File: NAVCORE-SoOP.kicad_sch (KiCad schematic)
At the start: 195 parts, among them J1 USB-C, J11 SERIAL2 4P, J12 U.FL ANT, J14 FLOW 6P, J15 LED 3P, J16 BUZZ 2P, J17 SERVO 6P, J18 PYRO 2P, J19 SWD 4P, J2 ESC 8P, J20 TOUCH 2P, J3 GPS+I2C, J5 RC IN, J6 CAN 4P, J8 microSD, J9 I2C 4P, P41 TEL_5V, P44 TEL_PPS, P46 TEL_GND, P71 RF_5V, P72 RF_TX, P73 RF_RX, P74 RF_GND, Q1 AO3400A, Q3 AO3400A, Q4 WST4041, Q5 AO3400A, SW1 BOOT, SW2 RESET, U1 STM32H743VIT6, U10 TLV75533, U11 SN65HVD230, U12 USBLC6-2SC6, U13 MAX2112, U14 OPA2374, U17 74LVC1G17, U19 TMP119, U2 ICM-42688-P, U20 LMR33630A, U21 XC6206P332MR, U3 ICM-42605, U4 MS5611, U5 W25Q128JVSIQ, U8 LMR33630A, U9 AP2112K-3.3, Y1 8MHz, Y2 25MHz TCXO

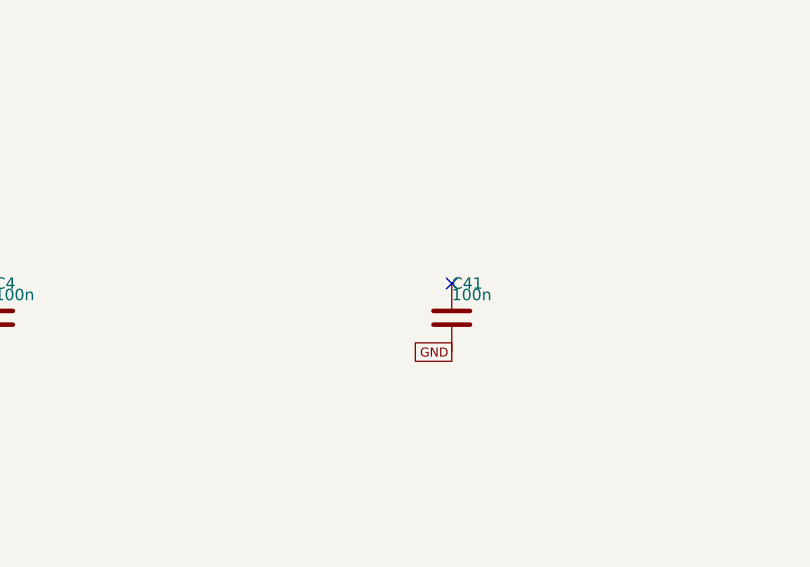
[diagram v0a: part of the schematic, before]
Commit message: give the payload and analogue rails real copper, put C41 on the CAN supply
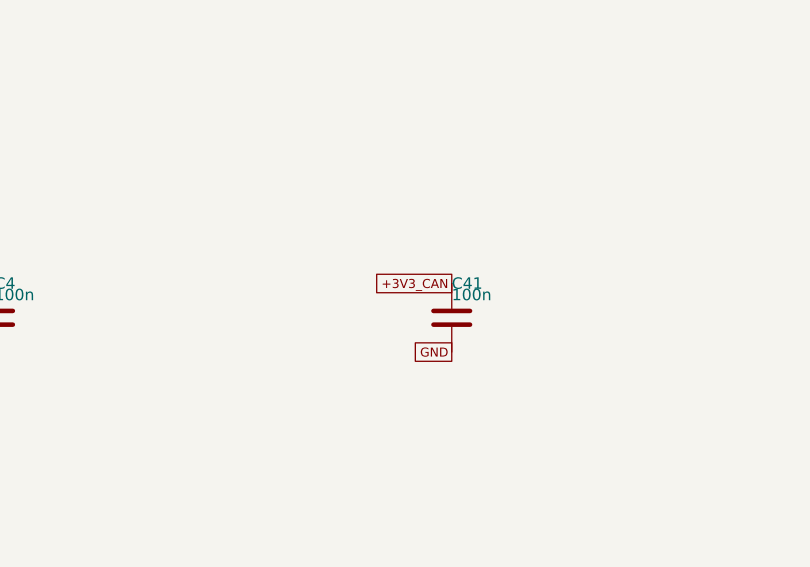
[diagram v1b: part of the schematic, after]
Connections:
- net +3V3_CAN: now also C41.1
- no-connect marks 44 -> 43
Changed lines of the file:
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@@
 		(instances (project "NAVCORE-SoOP" (path "/" (reference "C41") (unit 1))))
 	)
-	(no_connect (at 153.67 252.73))
+	(global_label "+3V3_CAN" (shape passive) (at 153.67 252.73 180)
+		(effects (font (size 1.0 1.0)) (justify right))
+	)
 	(global_label "GND" (shape passive) (at 153.67 260.35 180)
 		(effects (font (size 1.0 1.0)) (justify right))

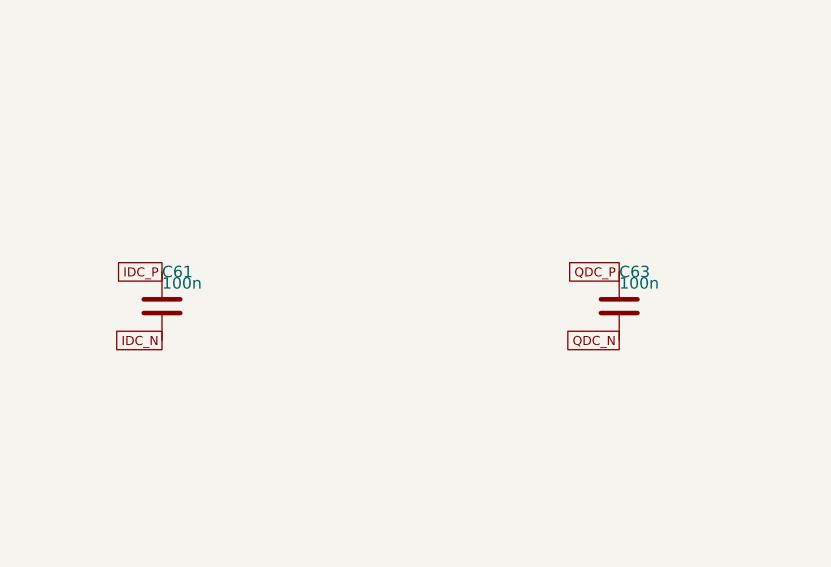
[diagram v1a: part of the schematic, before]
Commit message: fit 47 nF on the MAX2112 offset caps, as the datasheet asks
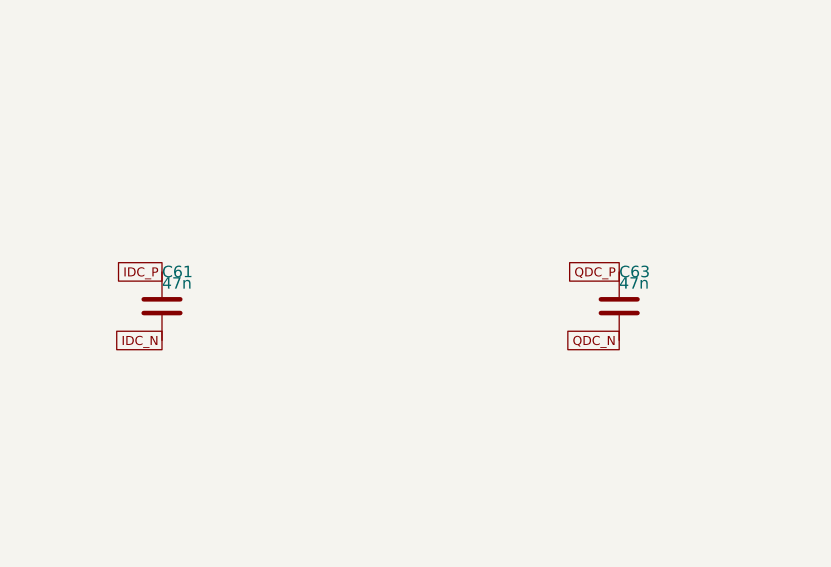
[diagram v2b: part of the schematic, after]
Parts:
- C61, C63: value 100n -> 47n
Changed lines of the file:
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@@
 		(exclude_from_sim no) (in_bom yes) (on_board yes) (dnp no)
 		(property "Reference" "C61" (at 1017.27 252.73 0) (effects (font (size 1.27 1.27)) (justify left)))
-		(property "Value" "100n" (at 1017.27 254.00 0) (effects (font (size 1.27 1.27)) (justify left)))
+		(property "Value" "47n" (at 1017.27 254.00 0) (effects (font (size 1.27 1.27)) (justify left)))
 		(property "Footprint" "Capacitor_SMD:C_0402_1005Metric" (at 1017.27 256.54 0) (effects (font (size 1.27 1.27)) hide))
 		(property "LCSC" "C1525" (at 1017.27 256.54 0) (effects (font (size 1.27 1.27)) hide))
@@
 		(exclude_from_sim no) (in_bom yes) (on_board yes) (dnp no)
 		(property "Reference" "C63" (at 1068.07 252.73 0) (effects (font (size 1.27 1.27)) (justify left)))
-		(property "Value" "100n" (at 1068.07 254.00 0) (effects (font (size 1.27 1.27)) (justify left)))
+		(property "Value" "47n" (at 1068.07 254.00 0) (effects (font (size 1.27 1.27)) (justify left)))
 		(property "Footprint" "Capacitor_SMD:C_0402_1005Metric" (at 1068.07 256.54 0) (effects (font (size 1.27 1.27)) hide))
 		(property "LCSC" "C1525" (at 1068.07 256.54 0) (effects (font (size 1.27 1.27)) hide))

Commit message: stop the artwork carrying part numbers that nothing checks
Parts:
- C61, C63: LCSC C1525 -> C82219
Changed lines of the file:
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@@
 		(property "Value" "47n" (at 1017.27 254.00 0) (effects (font (size 1.27 1.27)) (justify left)))
 		(property "Footprint" "Capacitor_SMD:C_0402_1005Metric" (at 1017.27 256.54 0) (effects (font (size 1.27 1.27)) hide))
-		(property "LCSC" "C1525" (at 1017.27 256.54 0) (effects (font (size 1.27 1.27)) hide))
+		(property "LCSC" "C82219" (at 1017.27 256.54 0) (effects (font (size 1.27 1.27)) hide))
 		(pin "1")
 		(pin "2")
@@
 		(property "Value" "47n" (at 1068.07 254.00 0) (effects (font (size 1.27 1.27)) (justify left)))
 		(property "Footprint" "Capacitor_SMD:C_0402_1005Metric" (at 1068.07 256.54 0) (effects (font (size 1.27 1.27)) hide))
-		(property "LCSC" "C1525" (at 1068.07 256.54 0) (effects (font (size 1.27 1.27)) hide))
+		(property "LCSC" "C82219" (at 1068.07 256.54 0) (effects (font (size 1.27 1.27)) hide))
 		(pin "1")
 		(pin "2")

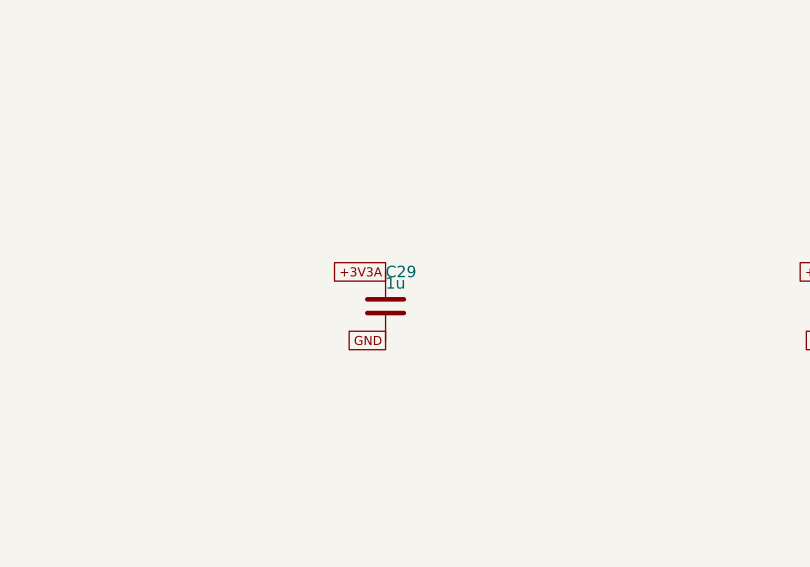
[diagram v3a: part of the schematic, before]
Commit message: widen C29 to 2u2 and sync the LCSC properties
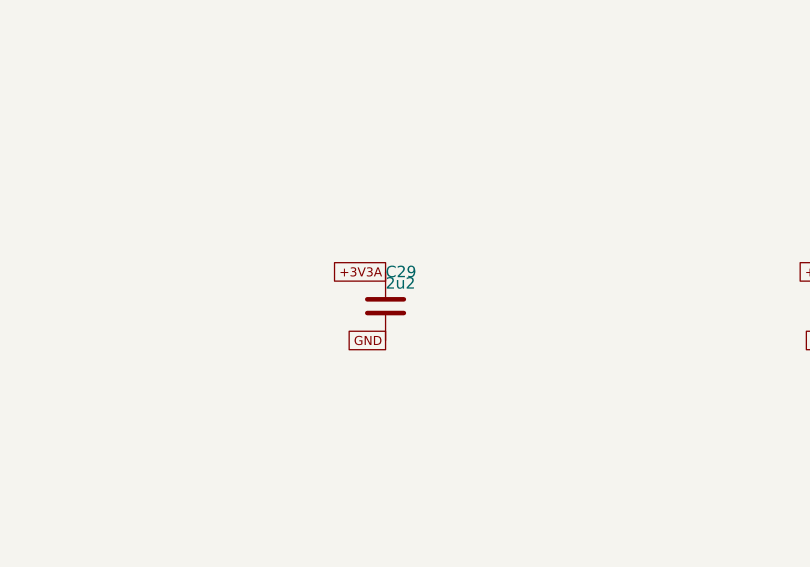
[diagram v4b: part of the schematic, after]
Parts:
- C29: value 1u -> 2u2; LCSC C52923 -> C12530
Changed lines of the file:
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@@
 		(exclude_from_sim no) (in_bom yes) (on_board yes) (dnp no)
 		(property "Reference" "C29" (at 999.49 207.01 0) (effects (font (size 1.27 1.27)) (justify left)))
-		(property "Value" "1u" (at 999.49 208.28 0) (effects (font (size 1.27 1.27)) (justify left)))
+		(property "Value" "2u2" (at 999.49 208.28 0) (effects (font (size 1.27 1.27)) (justify left)))
 		(property "Footprint" "Capacitor_SMD:C_0402_1005Metric" (at 999.49 210.82 0) (effects (font (size 1.27 1.27)) hide))
-		(property "LCSC" "C52923" (at 999.49 210.82 0) (effects (font (size 1.27 1.27)) hide))
+		(property "LCSC" "C12530" (at 999.49 210.82 0) (effects (font (size 1.27 1.27)) hide))
 		(pin "1")
 		(pin "2")

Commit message: hold the pyro gate down with 10 nF, load-test the bucks on the bench
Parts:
- added C87: 10n, Capacitor_SMD:C_0402_1005Metric, symbol Device:C
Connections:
- net GND: now also C87.2
- net PYRO_GATE: now also C87.1

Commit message: re-lay with latching GH ports and ESD on every lead
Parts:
- removed J11: SERIAL2 4P, jlc:CONN-SMD_4P-P1.00_SM04B-SRSS-TB-LF-SN, symbol jlc_parts:SM04B-SRSS-TB_(LF)(SN)
- removed J5: RC IN, jlc:CONN-SMD_4P-P1.00_SM04B-SRSS-TB-LF-SN, symbol jlc_parts:SM04B-SRSS-TB_(LF)(SN)
- removed J6: CAN 4P, jlc:CONN-SMD_4P-P1.00_SM04B-SRSS-TB-LF-SN, symbol jlc_parts:SM04B-SRSS-TB_(LF)(SN)
- removed J9: I2C 4P, jlc:CONN-SMD_4P-P1.00_SM04B-SRSS-TB-LF-SN, symbol jlc_parts:SM04B-SRSS-TB_(LF)(SN)
- removed PL1: LED_DIN, TestPoint:TestPoint_Pad_1.5x1.5mm, symbol Connector:TestPoint
- removed PL2: LED_5V, TestPoint:TestPoint_Pad_1.5x1.5mm, symbol Connector:TestPoint
- removed PL3: LED_GND, TestPoint:TestPoint_Pad_1.5x1.5mm, symbol Connector:TestPoint
- removed PZ1: BUZZ+, TestPoint:TestPoint_Pad_1.5x1.5mm, symbol Connector:TestPoint
- removed PZ2: BUZZ-, TestPoint:TestPoint_Pad_1.5x1.5mm, symbol Connector:TestPoint
- removed U5: W25Q128JVSIQ, jlc:SOIC-8_L5.3-W5.3-P1.27-LS8.0-BL, symbol jlc_parts:W25Q128JVSIQTR
- removed U9: AP2112K-3.3, jlc:SOT-25-5_L2.9-W1.6-P0.95-LS2.8-BL, symbol jlc_parts:AP2112K-3_3TRG1
- added C88, C89: 100n, Capacitor_SMD:C_0402_1005Metric, symbol Device:C
- added D6: PESD2CANFD24LT, jlc:SOT-23-3_L2.9-W1.6-P1.90-LS2.8-BR, symbol jlc_parts:PESD2CANFD24LT-QR
- added FID1, FID2, FID3: Fiducial, Fiducial:Fiducial_1mm_Mask2mm, symbol Mechanical:Fiducial
- added J11: SERIAL2 4P, jlc:CONN-SMD_4P-P1.25_BX-GH1.25-4PWT, symbol jlc_parts:BX-GH1_25-4PWT
- added J5: RC IN, jlc:CONN-SMD_4P-P1.25_BX-GH1.25-4PWT, symbol jlc_parts:BX-GH1_25-4PWT
- added J6: CAN 4P, jlc:CONN-SMD_4P-P1.25_BX-GH1.25-4PWT, symbol jlc_parts:BX-GH1_25-4PWT
- added J9: I2C 4P, jlc:CONN-SMD_4P-P1.25_BX-GH1.25-4PWT, symbol jlc_parts:BX-GH1_25-4PWT
- added U22, U23: SRV05-4, jlc:SOT-23-6_L2.9-W1.6-P0.95-LS2.8-BR, symbol jlc_parts:SRV05-4-P-T7_C6454456
- added U5: W25Q128JVPIQ, jlc:WSON-8-1EP_6x5mm_P1.27mm_EP3.4x4.3mm, symbol jlc_parts:W25Q128JVPIQTR
- added U9: TLV75733P, jlc:SOT-23-5_L2.9-W1.6-P0.95-LS2.8-BL-EP, symbol jlc_parts:TLV75733PDYDR
- J12: footprint Connector_Coaxial:U.FL_Hirose_U.FL-R-SMT-1_Vertical -> jlc:U.FL_Hirose_U.FL-R-SMT-1_Vertical_6L
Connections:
- net +3V3: now also U5.3 (#WP/IO2), U5.7 (#HOLD-OR-#REST/IO3), U5.8 (VCC), U9.5 (OUT)
- net +5V: now also C88.1, C89.1, J5.1, J9.1, U22.5 (Vcc), U23.5 (Vcc), U9.1 (IN), U9.3 (EN)
- net +5V_PAYLOAD: now also J11.1, J6.1
- net CANH: now also D6.1 (C), J6.2
- net CANL: now also D6.2 (C), J6.3
- net EXT_CS2: now also U5.1 (#CS)
- net GND: now also C88.2, C89.2, D6.3 (A), J11.4, J11.5, J11.6, J5.4, J5.5, J5.6, J6.4, J6.5, J6.6, J9.4, J9.5, J9.6, U22.2 (GND), U23.2 (GND), U5.4 (GND), U5.9 (EP), U9.2 (GND), U9.6 (EP)
- net I2C1_SCL: now also J9.2, U22.4 (IO3)
- net I2C1_SDA: now also J9.3, U22.6 (IO4)
- net RC_IN: now also J5.3, U23.3 (IO2)
- net SPI3_MISO: now also U5.2 (DO/IO1)
- net SPI3_MOSI: now also U5.5 (DI/IO0)
- net SPI3_SCK: now also U5.6 (CLK)
- net USART1_RX: now also J11.3
- net USART1_TX: now also J11.2
- net USART2_RX: now also U22.3 (IO2)
- net USART2_TX: now also U22.1 (IO1)
- net USART6_TX: now also J5.2, U23.1 (IO1)
- no-connect marks 43 -> 45

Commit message: model the mated plugs in the stack and re-lay Rev C to fit
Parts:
- removed C87: 10n, Capacitor_SMD:C_0402_1005Metric, symbol Device:C
- removed D5: 1N4148W, jlc:SOD-123F_L2.7-W1.6-LS3.8-RD, symbol jlc_parts:1N4148W_C81598
- removed F1: 3A, Fuse:Fuse_1206_3216Metric, symbol Device:Polyfuse_Small
- removed J15: LED 3P, jlc:CONN-SMD_3P-P1.00_SH1.0MM-3P-WT, symbol jlc_parts:SH1_0MM-3P-WT
- removed J16: BUZZ 2P, jlc:CONN-SMD_2P-P1.00_SM02B-SRSS-TB-LF-SN, symbol jlc_parts:SM02B-SRSS-TB_(LF)(SN)
- removed J18: PYRO 2P, jlc:CONN-SMD_2P-P1.00_SM02B-SRSS-TB-LF-SN, symbol jlc_parts:SM02B-SRSS-TB_(LF)(SN)
- removed J20: TOUCH 2P, jlc:CONN-SMD_2P-P1.00_SM02B-SRSS-TB-LF-SN, symbol jlc_parts:SM02B-SRSS-TB_(LF)(SN)
- removed Q5: AO3400A, jlc:SOT-23-3_L2.9-W1.3-P1.90-LS2.4-BR, symbol jlc_parts:AO3400A
- removed R54: 1k, Resistor_SMD:R_0402_1005Metric, symbol Device:R
- removed R55: 47k, Resistor_SMD:R_0402_1005Metric, symbol Device:R
- removed R56: 10k, Resistor_SMD:R_0402_1005Metric, symbol Device:R
- removed TP1: SWDIO, TestPoint:TestPoint_Pad_1.5x1.5mm, symbol Connector:TestPoint
- removed TP2: SWCLK, TestPoint:TestPoint_Pad_1.5x1.5mm, symbol Connector:TestPoint
- removed TP20: SWD_GND, TestPoint:TestPoint_Pad_1.5x1.5mm, symbol Connector:TestPoint
- removed TP21: SWD_3V3, TestPoint:TestPoint_Pad_1.5x1.5mm, symbol Connector:TestPoint
- removed TP22: VSERVO, TestPoint:TestPoint_Pad_1.5x1.5mm, symbol Connector:TestPoint
- removed TP5: USART1_TX, TestPoint:TestPoint_Pad_1.5x1.5mm, symbol Connector:TestPoint
- removed TP6: USART1_RX, TestPoint:TestPoint_Pad_1.5x1.5mm, symbol Connector:TestPoint
- removed TP7: WS2812, TestPoint:TestPoint_Pad_1.5x1.5mm, symbol Connector:TestPoint
- removed TP8: BUZZER, TestPoint:TestPoint_Pad_1.5x1.5mm, symbol Connector:TestPoint
- added P151: LED_5V, TestPoint:TestPoint_Pad_1.5x1.5mm, symbol Connector:TestPoint
- added P152: LED_DIN, TestPoint:TestPoint_Pad_1.5x1.5mm, symbol Connector:TestPoint
- added P153: LED_GND, TestPoint:TestPoint_Pad_1.5x1.5mm, symbol Connector:TestPoint
- added P161: BUZ_5V, TestPoint:TestPoint_Pad_1.5x1.5mm, symbol Connector:TestPoint
- added P162: BUZ_OUT, TestPoint:TestPoint_Pad_1.5x1.5mm, symbol Connector:TestPoint
- added P163: BUZ_GND, TestPoint:TestPoint_Pad_1.5x1.5mm, symbol Connector:TestPoint
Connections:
- net +5V: now also P161.1
- net +5V_PAYLOAD: now also P151.1
- net BUZZ_DRAIN: now also P162.1
- net GND: now also P153.1, P163.1
- net WS2812_OUT: now also P152.1
- net PYRO_FIRE: no longer names the net of U1.33 (PC5)
- net TOUCHDOWN: no longer names the net of U1.57 (PD10)
- no-connect marks 45 -> 46

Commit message: rev D design: perimeter connectors, servo headers and an on-board antenna feed
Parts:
- removed J12: U.FL ANT, jlc:U.FL_Hirose_U.FL-R-SMT-1_Vertical_6L, symbol Connector:Conn_Coaxial
- removed J14: FLOW 6P, jlc:CONN-SMD_SH1.0MM-6P-WT, symbol jlc_parts:SH1_0MM-6P-WT
- removed J17: SERVO 6P, jlc:CONN-SMD_SH1.0MM-6P-WT, symbol jlc_parts:SH1_0MM-6P-WT
- removed J19: SWD 4P, jlc:CONN-SMD_4P-P1.00_SM04B-SRSS-TB-LF-SN, symbol jlc_parts:SM04B-SRSS-TB_(LF)(SN)
- removed J2: ESC 8P, jlc:CONN-TH_SM08B-SRSS-TB-LF-SN, symbol jlc_parts:SM08B-SRSS-TB(LF)(SN)
- removed P41: TEL_5V, TestPoint:TestPoint_Pad_1.5x1.5mm, symbol Connector:TestPoint
- removed P44: TEL_PPS, TestPoint:TestPoint_Pad_1.5x1.5mm, symbol Connector:TestPoint
- removed P46: TEL_GND, TestPoint:TestPoint_Pad_1.5x1.5mm, symbol Connector:TestPoint
- removed P71: RF_5V, TestPoint:TestPoint_Pad_1.5x1.5mm, symbol Connector:TestPoint
- removed P72: RF_TX, TestPoint:TestPoint_Pad_1.5x1.5mm, symbol Connector:TestPoint
- removed P73: RF_RX, TestPoint:TestPoint_Pad_1.5x1.5mm, symbol Connector:TestPoint
- removed P74: RF_GND, TestPoint:TestPoint_Pad_1.5x1.5mm, symbol Connector:TestPoint
- removed PV1: PAYLOAD_5V, TestPoint:TestPoint_Pad_1.5x1.5mm, symbol Connector:TestPoint
- removed PV2: PAYLOAD_GND, TestPoint:TestPoint_Pad_1.5x1.5mm, symbol Connector:TestPoint
- added C90, C94, C95, C96: 100n, Capacitor_SMD:C_0402_1005Metric, symbol Device:C
- added C91: 10p, Capacitor_SMD:C_0402_1005Metric, symbol Device:C
- added C92: 22u, Capacitor_SMD:C_1206_3216Metric, symbol Device:C
- added C93: 10u, Capacitor_SMD:C_0805_2012Metric, symbol Device:C
- added D7: PESD5V0C1BSF, jlc:DSN0603-2_L0.6-W0.3-P0.40-BI, symbol Device:D_TVS
- added D8: PTVS5V0S1UR, jlc:SOD-123FL_L2.7-W1.8-LS3.8-RD, symbol jlc_parts:PTVS5V0S1UR
- added J12: MMCX-KWE-90, jlc:MMCX-TH_DL-MMCX-KWE-90, symbol jlc_parts:DL-MMCX-KWE-90
- added J14: FLOW 6P, jlc:CONN-SMD_XY-SM06B-GHS-TB, symbol jlc_parts:XY-SM06B-GHS-TB
- added J17: SERVO1, jlc:HDR-SMD_3P-P2.54-H-M_KH-2.54PH-1X3P-L13.5-WT, symbol jlc_parts:KH-2_54PH-1X3P-L13_5-WT
- added J19: TC2030-NL, Connector:Tag-Connect_TC2030-IDC-NL_2x03_P1.27mm_Vertical, symbol Connector:TC2030
- added J2: ESC 8P, jlc:CONN-SMD_SM08B-GHS-TB-LF-SN, symbol jlc_parts:SM08B-GHS-TB(LF)(SN)
- added J21: COMPANION, jlc:CONN-SMD_XY-SM06B-GHS-TB, symbol jlc_parts:XY-SM06B-GHS-TB
- added J22: PAYLOAD 5V, jlc:CONN-TH_SM03B-GHS-TB-LF-SN, symbol jlc_parts:SM03B-GHS-TB(LF)(SN)
- added J23: SERVO2, jlc:HDR-SMD_3P-P2.54-H-M_KH-2.54PH-1X3P-L13.5-WT, symbol jlc_parts:KH-2_54PH-1X3P-L13_5-WT
- added L6: 27nH, jlc:L0402, symbol Device:L
- added R59, R60: 10k, Resistor_SMD:R_0402_1005Metric, symbol Device:R
- added R61: 210k, Resistor_SMD:R_0402_1005Metric, symbol Device:R
- added R62: 2R2, Resistor_SMD:R_0402_1005Metric, symbol Device:R
- added U24: AP22653, jlc:SOT-23-6_L2.9-W1.6-P0.95-LS2.8-BR, symbol jlc_parts:AP22653W6-7
- added U25: INA180A2, jlc:SOT-23-5_L3.0-W1.7-P0.95-LS2.8-BL, symbol jlc_parts:INA180A2IDBVR
- FID1, FID2, FID3, P151, P152, P153, P161, P162, P163, TP10, TP3, TP4, TP9: now left out of the parts list
- L5: footprint Inductor_SMD:L_APV_ANR4030 -> Inductor_SMD:L_APV_ANR5040; LCSC C167879 -> C354610
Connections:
- net +3V3: now also C94.1, J14.1, J19.1, R60.1, U25.5 (VS)
- net +5V: now also C95.1, J21.1, R59.1, U24.1 (IN)
- net +5V_PAYLOAD: now also C92.1, D8.1 (K), J17.2, J22.1, J23.2
- net ANT_IN: now also D7.1 (A1), J12.1 (SIG), L6.2
- net ESC_CUR: now also J2.7
- net ESC_TEL: now also J2.8
- net EXT_CS1: now also J14.5
- net GND: now also C90.2, C91.2, C92.2, C93.2, C94.2, C95.2, C96.2, D7.2 (A2), D8.2 (A), J12.2 (GND), J12.3 (GND), J12.4 (GND), J12.5 (GND), J14.6, J14.7, J14.8, J17.3, J19.5, J19.6, J2.1, J2.10, J2.9, J21.6, J21.7, J21.8, J22.2, J22.3, J22.4, J22.5, J23.3, R61.2, U24.2 (GND), U25.2 (GND)
- net M1: now also J2.3
- net M2: now also J2.4
- net M3: now also J2.5
- net M4: now also J2.6
- net NRST: now also J19.3
- net PWM7: now also J17.1
- net PWM8: now also J23.1
- net SPI3_MISO: now also J14.3
- net SPI3_MOSI: now also J14.4
- net SPI3_SCK: now also J14.2
- net SWCLK: now also J19.4
- net SWDIO: now also J19.2
- net VBAT_IN: now also J2.2
- net ANT_CURRENT: now reaches U1.17 (PC2_C)
- net ANT_CURRENT: now also U25.1 (OUT)
- net BIAS_EN: now reaches U1.33 (PC5)
- net BIAS_EN: now also R59.2, U24.3 (EN/EN#)
- net UART7_RX: now reaches U1.37 (PE7)
- net UART7_RX: now also J21.3
- net UART7_TX: now reaches U1.38 (PE8)
- net UART7_TX: now also J21.2
- net UART7_RTS: now reaches U1.39 (PE9)
- net UART7_RTS: now also J21.5
- net BIAS_FAULT: now reaches U1.57 (PD10)
- net BIAS_FAULT: now also R60.2, U24.4 (FAULT#)
- net PPS_SYNC renamed UART7_CTS
- net UART7_CTS: now also J21.4
- net PWM10: no longer names the net of U1.62 (PD15)
- net PWM9: no longer names the net of U1.61 (PD14)
- net UART4_RX: no longer names the net of U1.95 (PB8)
- net UART4_TX: no longer names the net of U1.96 (PB9)
- new net +5V_BIAS: C90.1, C91.1, C93.1, L6.1, R62.2, U25.4 (IN-)
- new net +5V_BIAS_SW: C96.1, R62.1, U24.6 (OUT), U25.3 (IN+)
- new net BIAS_ILIM: R61.1, U24.5 (ILIM)
- no-connect marks 46 -> 44
